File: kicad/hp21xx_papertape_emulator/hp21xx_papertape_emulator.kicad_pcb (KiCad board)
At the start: 2 copper layers, 66.5 x 77.4 mm, 192 parts, among them J1 SWD, J2 SERIAL, J3 Micro_SD_Card_Det_Hirose_DM3AT, J5 Conn_02x13_Odd_Even, Q1 BSS138, Q10 BSS138, Q11 BSS138, Q12 BSS84, Q13 BSS138, Q14 BSS138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

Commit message: Fixed missing LCSC number for BAT54
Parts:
- renumbered Re to R42

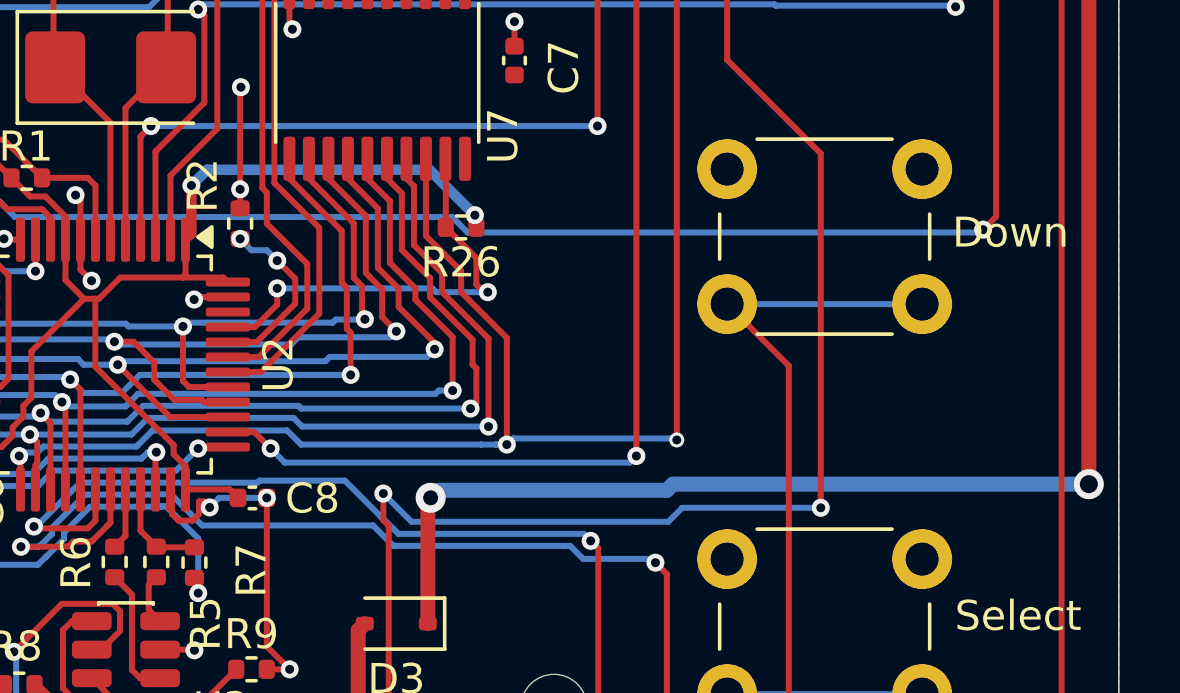
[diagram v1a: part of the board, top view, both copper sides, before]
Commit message: Added jumper to be able to use serial bootstrap mode.
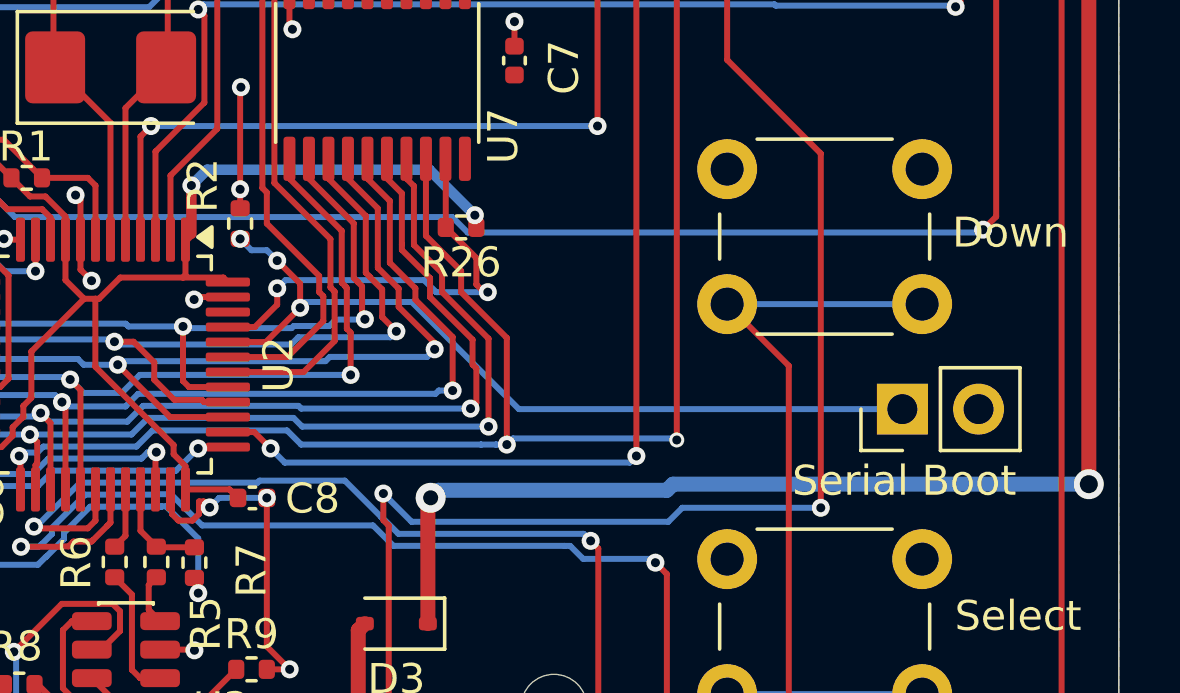
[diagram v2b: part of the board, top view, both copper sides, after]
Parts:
- added Serial Boot: Serial boot when bridged, Connector_PinHeader_2.54mm:PinHeader_1x02_P2.54mm_Vertical, F.Cu at (148.2, 134.2)
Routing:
- net Net-(JP1-A): track 5.99 -> 27.9 mm, vias 2 -> 3
- net Net-(OLED1-SCL): track 24.6 -> 25.9 mm
- net Net-(OLED1-SDA): track 20.1 -> 21.2 mm
